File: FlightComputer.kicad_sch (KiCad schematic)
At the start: 79 parts, among them J1 Conn_01x05_Pin, J10 503182-1852, J2 Conn_01x03_Pin, J3 Conn_01x06_Pin, J4 Conn_01x03_Pin, J5 Conn_01x03, J6 Conn_01x03, J7 Screw_Terminal_01x02, J8 Screw_Terminal_01x02, J9 Conn_ST_STDC14, Q1 2N7002, Q2 2N7002, Q3 IRFR9120N, Q4 IRFR9120N, U1 BMM350, U2 INA260, U3 BMP581, U5 ICM-45686, U6 STM32F722RETx, U7 STM32H757XIHx, Y1 25MHz, Y2 32.768kHz

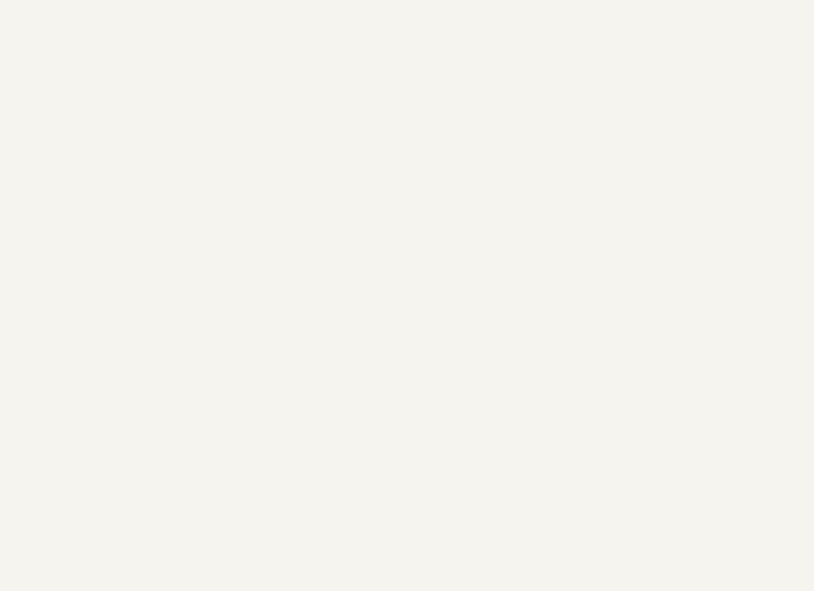
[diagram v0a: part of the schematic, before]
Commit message: Added GPS
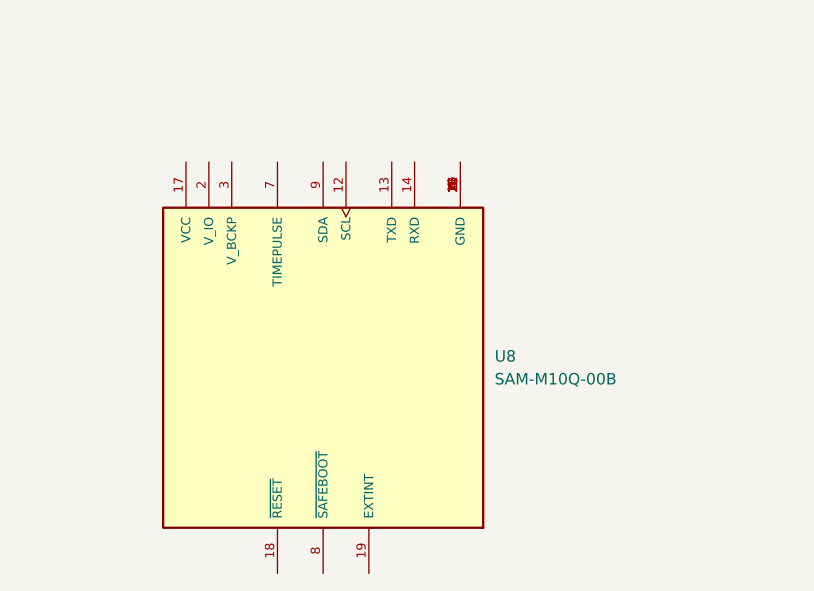
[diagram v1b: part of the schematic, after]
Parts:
- added U8: SAM-M10Q-00B, SAM-M10Q-00B:XCVR_SAM-M10Q-00B, symbol SAM-M10Q-00B:SAM-M10Q-00B
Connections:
- new net: U8.1 (GND), U8.10 (GND), U8.11 (GND), U8.15 (GND), U8.16 (GND), U8.20 (GND), U8.4 (GND), U8.5 (GND), U8.6 (GND)
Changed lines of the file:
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@@
+	)
+	(symbol
+		(lib_id "SAM-M10Q-00B:SAM-M10Q-00B")
+		(at 278.13 332.74 90)
+		(unit 1)
+		(exclude_from_sim no)
+		(in_bom yes)
+		(on_board yes)
+		(dnp no)
+		(fields_autoplaced yes)
+		(property "Reference" "U8"
+			(at 297.18 331.4699 90)
+			(effects
+				(font
+					(size 1.27 1.27)
+				)
+				(justify right)
+			)
+		)
+		(property "Value" "SAM-M10Q-00B"
+			(at 297.18 334.0099 90)
+			(effects
+				(font
+					(size 1.27 1.27)
+				)
+				(justify right)
+			)
+		)
+		(property "Footprint" "SAM-M10Q-00B:XCVR_SAM-M10Q-00B"
+			(at 278.13 332.74 0)
+			(effects
+				(font
+					(size 1.27 1.27)
+				)
+				(justify bottom)
+				(hide yes)
+			)
+		)
+		(property "Datasheet" ""
+			(at 278.13 332.74 0)
+			(effects
+				(font
+					(size 1.27 1.27)
+				)
+				(hide yes)
+			)
+		)
+		(property "Description" ""
+			(at 278.13 332.74 0)
+			(effects
+				(font
+					(size 1.27 1.27)
+				)
+				(hide yes)
+			)
+		)
+		(property "MF" "u-blox"
+			(at 278.13 332.74 0)
+			(effects
+				(font
+					(size 1.27 1.27)
+				)
+				(justify bottom)
+				(hide yes)
+			)
+		)
+		(property "MAXIMUM_PACKAGE_HEIGHT" "6.8mm"
+			(at 278.13 332.74 0)
+			(effects
+				(font
+					(size 1.27 1.27)
+				)
+				(justify bottom)
+				(hide yes)
+			)
+		)
+		(property "Package" "None"
+			(at 278.13 332.74 0)
+			(effects
+				(font
+					(size 1.27 1.27)
+				)
+				(justify bottom)
+				(hide yes)
+			)
+		)
+		(property "Price" "None"
+			(at 278.13 332.74 0)
+			(effects
+				(font
+					(size 1.27 1.27)
+				)
+				(justify bottom)
+				(hide yes)
+			)
+		)
+		(property "Check_prices" "https://www.snapeda.com/parts/SAM-M10Q-00B/u-blox/view-part/?ref=eda"
+			(at 278.13 332.74 0)
+			(effects
+				(font
+					(size 1.27 1.27)
+				)
+				(justify bottom)
+				(hide yes)
+			)
+		)
+		(property "STANDARD" "Manufacturer Recommendations"
+			(at 278.13 332.74 0)
+			(effects
+				(font
+					(size 1.27 1.27)
+				)
+				(justify bottom)
+				(hide yes)
+			)
+		)
+		(property "PARTREV" "R03"
+			(at 278.13 332.74 0)
+			(effects
+				(font
+					(size 1.27 1.27)
+				)
+				(justify bottom)
+				(hide yes)
+			)
+		)
+		(property "SnapEDA_Link" "https://www.snapeda.com/parts/SAM-M10Q-00B/u-blox/view-part/?ref=snap"
+			(at 278.13 332.74 0)
+			(effects
+				(font
+					(size 1.27 1.27)
+				)
+				(justify bottom)
+				(hide yes)
+			)
+		)
+		(property "MP" "SAM-M10Q-00B"
+			(at 278.13 332.74 0)
+			(effects
+				(font
+					(size 1.27 1.27)
+				)
+				(justify bottom)
+				(hide yes)
+			)
+		)
+		(property "Description_1" "- RF Receiver Galileo, GLONASS, GPS 1.575GHz, 1.602GHz -165dBm 400kbps On-Board, Patch Module"
+			(at 278.13 332.74 0)
+			(effects
+				(font
+					(size 1.27 1.27)
+				)
+				(justify bottom)
+				(hide yes)
+			)
+		)
+		(property "SNAPEDA_PN" "SAM-M10Q-00B"
+			(at 278.13 332.74 0)
+			(effects
+				(font
+					(size 1.27 1.27)
+				)
+				(justify bottom)
+				(hide yes)
+			)
+		)
+		(property "Availability" "In Stock"
+			(at 278.13 332.74 0)
+			(effects
+				(font
+					(size 1.27 1.27)
+				)
+				(justify bottom)
+				(hide yes)
+			)
+		)
+		(property "MANUFACTURER" "u-blox"
+			(at 278.13 332.74 0)
+			(effects
+				(font
+					(size 1.27 1.27)
+				)
+				(justify bottom)
+				(hide yes)
+			)
+		)
+		(pin "17"
+		)
+		(pin "7"
+		)
+		(pin "10"
+		)
+		(pin "11"
+		)
+		(pin "1"
+		)
+		(pin "9"
+		)
+		(pin "3"
+		)
+		(pin "14"
+		)
+		(pin "15"
+		)
+		(pin "8"
+		)
+		(pin "4"
+		)
+		(pin "16"
+		)
+		(pin "18"
+		)
+		(pin "12"
+		)
+		(pin "5"
+		)
+		(pin "19"
+		)
+		(pin "6"
+		)
+		(pin "13"
+		)
+		(pin "2"
+		)
+		(pin "20"
+		)
+		(instances
+			(project ""
+				(path "/5355eb0b-cf16-41a1-9b26-3d74ed8be4e2"
+					(reference "U8")
+					(unit 1)
+				)
+			)
+		)
 	)
 	(symbol

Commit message: added files for the schematic
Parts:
- removed C10, C14, C16, C17, C18, C20, C21: 100nF, Capacitor_SMD:C_0603_1608Metric, symbol Device:C
- removed C15: 100nF, Capacitor_SMD:C_0402_1005Metric, symbol Device:C
- removed C19: 4.7uF, Capacitor_SMD:C_0603_1608Metric, symbol Device:C
- removed C22: 10nF, Capacitor_SMD:C_0603_1608Metric, symbol Device:C
- removed C23, C24: 1uF, Capacitor_SMD:C_0603_1608Metric, symbol Device:C
- removed FB1: 100R, Inductor_SMD:L_0603_1608Metric, symbol Device:FerriteBead
- removed R1: 100k, Resistor_SMD:R_0603_1608Metric, symbol Device:R
- removed R10, R11: 10k, Resistor_SMD:R_0402_1005Metric, symbol Device:R
- removed R15, R16: 4.7k, Resistor_SMD:R_0402_1005Metric, symbol Device:R
- removed U5: ICM-45686, ICM-45686:IC_ICM-45686, symbol ICM-45686:ICM-45686
- removed U6: STM32F722RETx, Package_QFP:LQFP-64_10x10mm_P0.5mm, symbol MCU_ST_STM32F7:STM32F722RETx
- added C28, C29, C30, C31, C32, C33, C34, C35, C36, C37, C38, C39, C40, C41, C42, C43, C44, C45, C46, C47, C48, C50, C51, C56, C57: 100nF, Capacitor_SMD:C_0603_1608Metric, symbol Device:C
- added C49: 100nF, Capacitor_SMD:C_0402_1005Metric, symbol Device:C
- added C52, C58, C59: 10uF, Capacitor_SMD:C_0603_1608Metric, symbol Device:C
- added C53, C54, C55: 4.7uF, Capacitor_SMD:C_0603_1608Metric, symbol Device:C
- added C60, C61: 2.2uF, Capacitor_SMD:C_0603_1608Metric, symbol Device:C
- added C63: 10nF, Capacitor_SMD:C_0603_1608Metric, symbol Device:C
- added C64, C65: 1uF, Capacitor_SMD:C_0603_1608Metric, symbol Device:C
- added C66: 220pF, Capacitor_SMD:C_0603_1608Metric, symbol Device:C
- added FB3: 100R, Inductor_SMD:L_0603_1608Metric, symbol Device:FerriteBead
- added L1: 2.2uH, symbol Device:L
- added R23: 100k, Resistor_SMD:R_0603_1608Metric, symbol Device:R
- added R24, R25: 4.7k, Resistor_SMD:R_0603_1608Metric, symbol Device:R
- added R26, R27: 10k, Resistor_SMD:R_0603_1608Metric, symbol Device:R
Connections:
- net IMU_SCL is gone; now on net I2C3_SCL: U1.A3 (SCK), U4.13 (SCL)
- net IMU_SDA is gone; now on net I2C3_SDA: U1.A2 (SDA), U4.14 (SDA)
- net UART2_RX is gone; now on net UART4_RX: J2.2 (Pin_2)
- net UART2_TX is gone; now on net UART4_TX: J2.1 (Pin_1)
- net 3V3: now also U7.A6 (VDDLDO), U7.B1 (VBAT), U7.C17 (VDDLDO), U7.E11 (VDD), U7.E6 (VDD), U7.E7 (PDR_ON), U7.E9 (VDD), U7.F1 (VDDSMPS), U7.F17 (VDD33_USB), U7.F5 (VDD), U7.G13 (VDD), U7.G17 (VDD50_USB), U7.G5 (VDD), U7.H13 (VDD), U7.H5 (VDD), U7.J13 (VDD), U7.K13 (VDD), U7.K5 (VDD), U7.L13 (VDD), U7.L5 (VDD), U7.M13 (VDD), U7.M5 (VDD), U7.N10 (VDD), U7.N11 (VDD), U7.N12 (VDD), U7.N7 (VDD), U7.N8 (VDD), U7.P17 (VDDDSI), U7.U12 (VDDLDO), C28.1, C29.1, C30.1, C31.1, C32.1, C33.1, C34.1, C35.1, C36.1, C37.1, C38.1, C39.1, C40.1, C41.1, C42.1, C43.1, C44.1, C45.1, C46.1, C47.1, C48.1, C50.1, C51.1, C52.1, C53.1, C54.1, C55.1, C56.1, C57.1, C65.1, FB3.2, R24.1, R25.1, R26.1, R27.1
- net DEPLOY: now also U7.U4 (PC5)
- net GND: now also U7.A1 (VSS), U7.A17 (VSS), U7.B2 (VSS), U7.B6 (VSS), U7.C10 (VSS), U7.C13 (VSS), U7.C16 (VSS), U7.F2 (VSSSMPS), U7.G10 (VSS), U7.G11 (VSS), U7.G16 (VSS), U7.G7 (VSS), U7.G8 (VSS), U7.G9 (VSS), U7.H10 (VSS), U7.H11 (VSS), U7.H7 (VSS), U7.H8 (VSS), U7.H9 (VSS), U7.J10 (VSS), U7.J11 (VSS), U7.J16 (VSS), U7.J17 (VSS), U7.J3 (VSS), U7.J7 (VSS), U7.J8 (VSS), U7.J9 (VSS), U7.K10 (VSS), U7.K11 (VSS), U7.K15 (VSSDSI), U7.K7 (VSS), U7.K8 (VSS), U7.K9 (VSS), U7.L10 (VSS), U7.L11 (VSS), U7.L15 (VSSDSI), U7.L7 (VSS), U7.L8 (VSS), U7.L9 (VSS), U7.M15 (VSSDSI), U7.N1 (VREF-), U7.N16 (VSS), U7.P1 (VSSA), U7.R4 (VSS), U7.R8 (VSS), U7.T12 (VSS), U7.U1 (VSS), U7.U17 (VSS), C28.2, C29.2, C30.2, C31.2, C32.2, C33.2, C34.2, C35.2, C36.2, C37.2, C38.2, C39.2, C40.2, C41.2, C42.2, C43.2, C44.2, C45.2, C46.2, C47.2, C48.2, C49.2, C50.2, C51.2, C52.2, C53.2, C54.2, C55.2, C56.2, C57.2, C58.2, C59.2, C60.2, C61.2, C63.2, C64.2, C65.2, C66.2, R23.2
- net HSE_IN: now also U7.J2 (PH0)
- net HSE_OUT: now also U7.J1 (PH1)
- net IGNITE: now also U7.U10 (PE14)
- net LSE_IN: now also U7.C2 (PC14)
- net LSE_OUT: now also U7.C1 (PC15)
- net SCL1: now also U7.B5 (PB6), R25.2
- net SDA1: now also U7.C5 (PB7), R24.2
- net SDMMC1_CLK: now also U7.C12 (PC12)
- net SDMMC1_CMD: now also U7.D12 (PD2)
- net SDMMC1_D0: now also U7.E13 (PC8)
- net SDMMC1_D1: now also U7.E14 (PC9)
- net SDMMC1_D2: now also U7.A13 (PC10)
- net SDMMC1_D3: now also U7.B13 (PC11)
- net SWDIO: now also U7.C15 (PA13)
- net UART4_RX: now also U7.T2 (PA1_C); no longer J4.2 (Pin_2)
- net UART4_TX: now also U7.T1 (PA0_C); no longer J4.1 (Pin_1)
- net ~{NRST}: now also U7.K1 (NRST), C49.1
- net at U7.A7 (VCAP): now also C60.1
- net SWCLK: now reaches U7.B14 (PA14)
- net at U7.D17 (VCAP): now also U7.U11 (VCAP), C61.1
- net at U7.E1 (VLXSMPS): now also C66.1, L1.1
- net at U7.E8 (BOOT0): now also R23.1
- net at U7.G2 (VFBSMPS): now also C58.1, C59.1, L1.2
- net VREF: now reaches U7.L1 (VDDA)
- net VREF: now also U7.M1 (VREF+), C63.1, C64.1, FB3.1
- net I2C3_SDA: now reaches U7.T13 (PH8)
- net I2C3_SDA: now also R26.2
- net I2C3_SCL: now reaches U7.U13 (PH7)
- net I2C3_SCL: now also R27.2
- net UART1_RX: no longer names the net of J9.14 (VCP_TX)
- net UART1_TX: no longer names the net of J9.13 (VCP_RX)
- no-connect marks 27 -> 19
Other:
- note removed: "Address: 0x68"
- title: Flight Computer -> TARS
- moved on the sheet: C11, C12, C25, C26, C27, C8, C9, D1, FB2, J10, J2, J5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

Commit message: updated
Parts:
- added C1, C3: 100nF, Capacitor_SMD:C_0402_1005Metric, symbol Device:C
- added C4: 100nF, Capacitor_SMD:C_0603_1608Metric, symbol Device:C
- C20: renamed from C59; footprint Capacitor_SMD:C_0603_1608Metric -> Capacitor_SMD:C_0402_1005Metric
- C21: renamed from C60; footprint Capacitor_SMD:C_0603_1608Metric -> Capacitor_SMD:C_0402_1005Metric
- C22: renamed from C58; footprint Capacitor_SMD:C_0603_1608Metric -> Capacitor_SMD:C_0402_1005Metric
- C23: renamed from C66; footprint Capacitor_SMD:C_0603_1608Metric -> Capacitor_SMD:C_0402_1005Metric
- C24: renamed from C61; footprint Capacitor_SMD:C_0603_1608Metric -> Capacitor_SMD:C_0402_1005Metric
- C27: renamed from C35; footprint Capacitor_SMD:C_0603_1608Metric -> Capacitor_SMD:C_0402_1005Metric
- C28: footprint Capacitor_SMD:C_0603_1608Metric -> Capacitor_SMD:C_0402_1005Metric
- C31: renamed from C36; footprint Capacitor_SMD:C_0603_1608Metric -> Capacitor_SMD:C_0402_1005Metric
- C32: renamed from C29; footprint Capacitor_SMD:C_0603_1608Metric -> Capacitor_SMD:C_0402_1005Metric
- C35: renamed from C37; footprint Capacitor_SMD:C_0603_1608Metric -> Capacitor_SMD:C_0402_1005Metric
- C36: renamed from C30; footprint Capacitor_SMD:C_0603_1608Metric -> Capacitor_SMD:C_0402_1005Metric
- C39: renamed from C38; footprint Capacitor_SMD:C_0603_1608Metric -> Capacitor_SMD:C_0402_1005Metric
- C40: renamed from C31; footprint Capacitor_SMD:C_0603_1608Metric -> Capacitor_SMD:C_0402_1005Metric
- C43: renamed from C39; footprint Capacitor_SMD:C_0603_1608Metric -> Capacitor_SMD:C_0402_1005Metric
- C44: renamed from C32; footprint Capacitor_SMD:C_0603_1608Metric -> Capacitor_SMD:C_0402_1005Metric
- C47: renamed from C40; footprint Capacitor_SMD:C_0603_1608Metric -> Capacitor_SMD:C_0402_1005Metric
- C48: renamed from C33; footprint Capacitor_SMD:C_0603_1608Metric -> Capacitor_SMD:C_0402_1005Metric
- C51: renamed from C41; footprint Capacitor_SMD:C_0603_1608Metric -> Capacitor_SMD:C_0402_1005Metric
- C52: renamed from C34; footprint Capacitor_SMD:C_0603_1608Metric -> Capacitor_SMD:C_0402_1005Metric
- C53: renamed from C52; value 10uF -> 4.7uF; footprint Capacitor_SMD:C_0603_1608Metric -> Capacitor_SMD:C_0402_1005Metric
- J5: renamed from J3; footprint Connector_JST:JST_PH_S6B-PH-SM4-TB_1x06-1MP_P2.00mm_Horizontal -> Connector_JST:JST_PH_S8B-PH-SM4-TB_1x08-1MP_P2.00mm_Horizontal
- L1: footprint (none) -> Capacitor_SMD:C_1812_4532Metric; JLCPCB (none) -> C86093
- renumbered C9 to C10, C2 to C11, C11 to C12, C5 to C13, C12 to C14, C6 to C15, C25 to C16, C26 to C17, C27 to C18, C49 to C19, C7 to C2, C50 to C25, C42 to C26, C51 to C29, C43 to C30, C53 to C33, C44 to C34, C54 to C37, C45 to C38, C55 to C41, C46 to C42, C56 to C45, C47 to C46, C57 to C49, C4 to C5, C48 to C50, C63 to C54, C64 to C55, C65 to C56, C13 to C6, C3 to C7, C1 to C8, C8 to C9, FB2 to FB1, FB3 to FB2, J5 to J3, J6 to J4, J4 to J6, J9 to J7, J7 to J8, J8 to J9, R20 to R1, R4 to R10, R5 to R11, R6 to R12, R7 to R13, R8 to R14, R9 to R15, R21 to R16, R22 to R17, R23 to R18, R27 to R19, R12 to R2, R26 to R20, R24 to R21, R25 to R22, R13 to R3, R14 to R4, R17 to R5, R18 to R6, R19 to R7, R2 to R8, R3 to R9, U4 to U1, U8 to U3, U1 to U4, U3 to U5, U7 to U6
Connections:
- net SWCLK is gone; now on net SWDCLK: U6.B14 (PA14)
- net GND: now also U3.1 (GND), U3.10 (GND), U3.11 (GND), U3.15 (GND), U3.16 (GND), U3.20 (GND), U3.4 (GND), U3.5 (GND), U3.6 (GND), C1.1, C3.1, C4.1
- net GNSS_RX: now reaches U3.13 (TXD)
- net GNSS_RX: now also U6.C4 (PE0)
- net GNSS_TX: now reaches U3.14 (RXD)
- net GNSS_TX: now also U6.B4 (PE1)
- net at U3.17 (VCC): now also U3.2 (V_IO), U3.3 (V_BCKP), C1.2, C3.2, C4.2
- net GNSS_RST: now reaches U3.18 (~{RESET})
- net BMM350_INT: now reaches U4.A1 (INT)
- net LSM_INT1: now reaches U1.4 (INT1)
- net LSM_INT2: now reaches U1.9 (INT2)
- net INA260_INT: now reaches U2.7 (ALERT)
- net BMP581_INT: now reaches U5.7 (INT)
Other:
- moved on the sheet: C10, C11, C12, C13, C14, C15, C16, C17, C18, C2, C5, C6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
